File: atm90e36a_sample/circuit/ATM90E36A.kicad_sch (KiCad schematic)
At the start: 23 parts, among them J1 Conn_01x05, U2 ATM90E36A-AU-R, Y1 16.384MHz

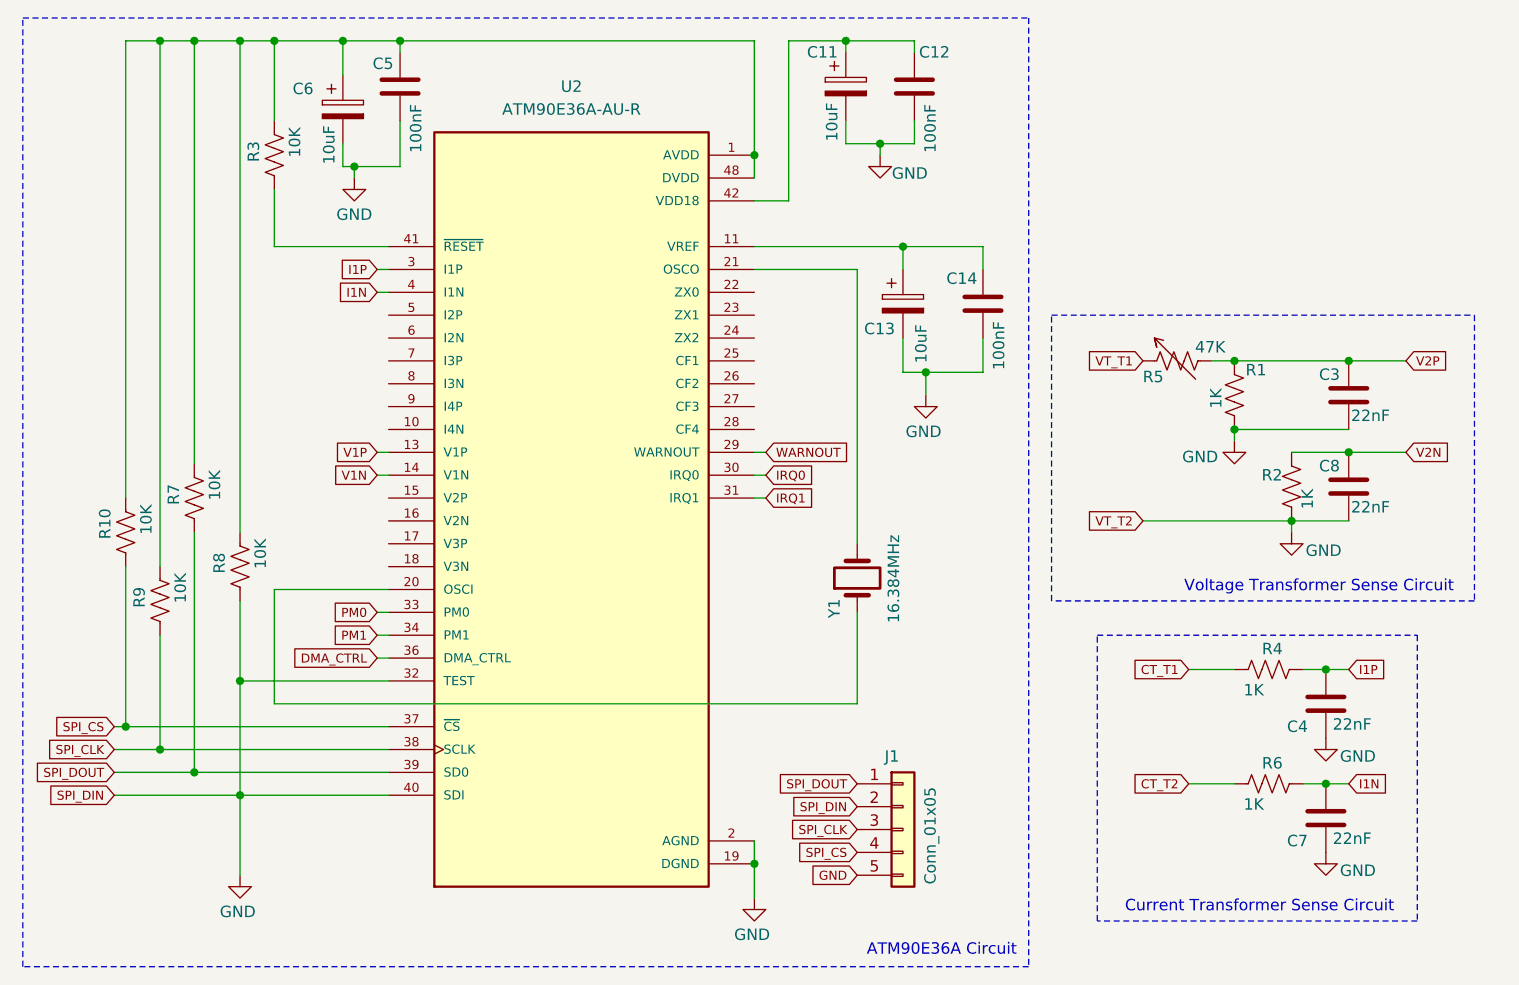
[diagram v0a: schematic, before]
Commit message: add ATM90E36A sample code and schematic after successful testing
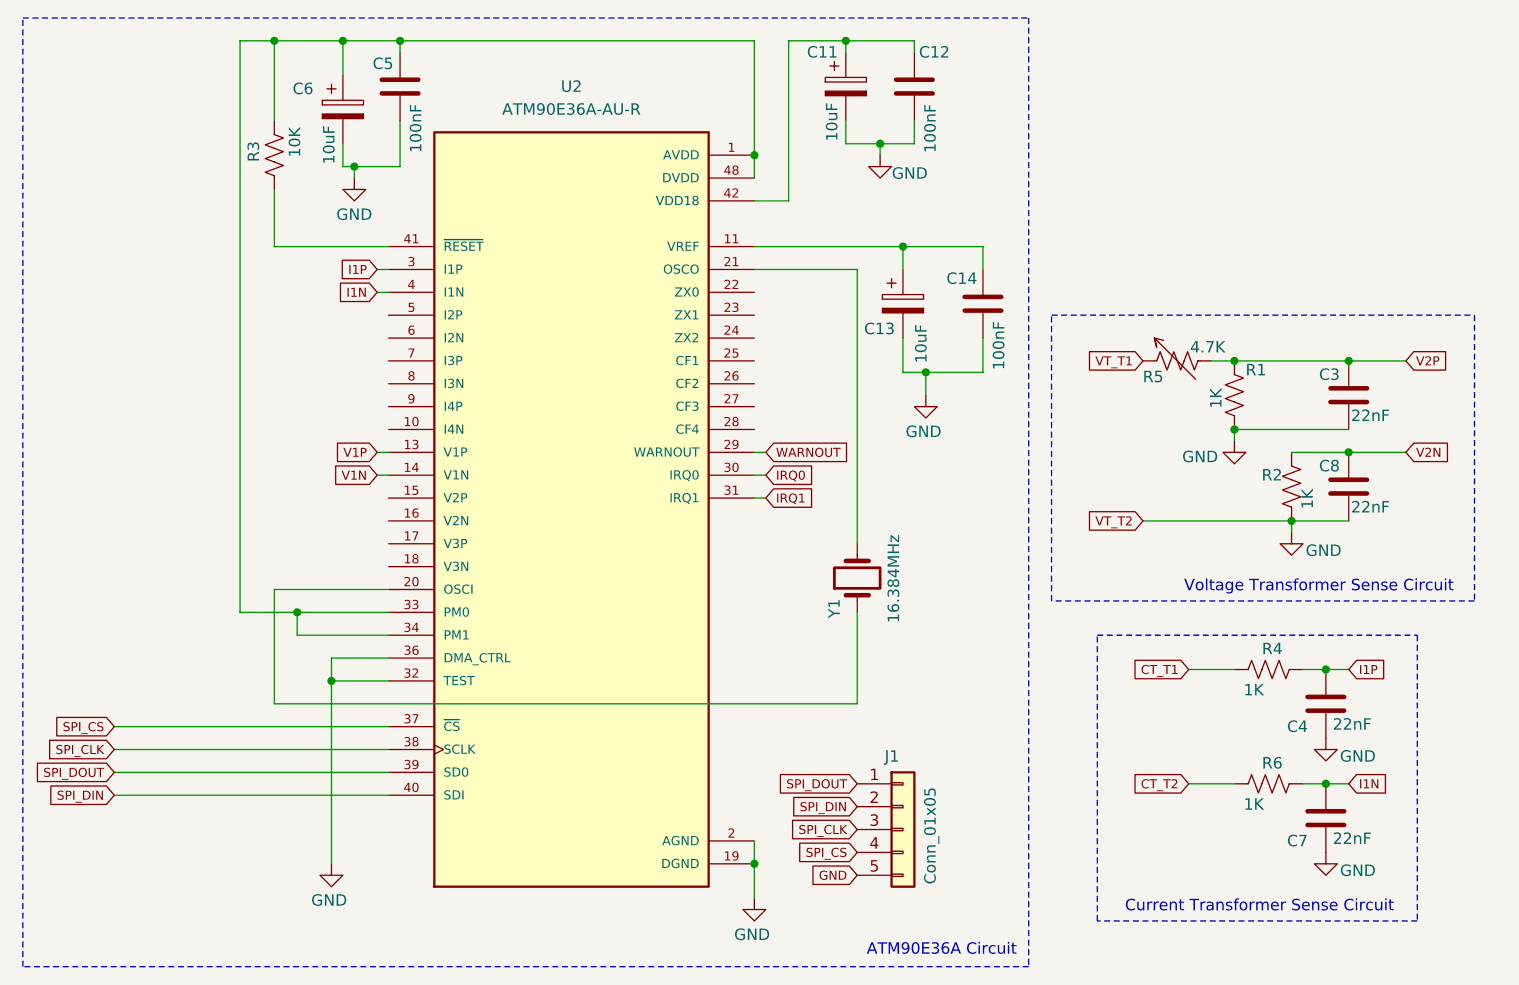
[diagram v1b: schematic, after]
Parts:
- removed R10, R7, R8, R9: 10K, symbol Device:R_US
- R5: value 47K -> 4.7K
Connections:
- net DMA_CTRL is gone; now on net AGND: U2.36 (DMA_CTRL)
- net PM0 is gone; now on an unnamed net: U2.33 (PM0)
- net PM1 is gone; now on an unnamed net: U2.34 (PM1)
- net AGND: no longer J1.2 (Pin_2), U2.40 (SDI)
- new net SPI_DIN: J1.2 (Pin_2), U2.40 (SDI)
